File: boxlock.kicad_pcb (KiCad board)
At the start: 2 copper layers, 49.2 x 82.2 mm, 39 parts, among them J2 SOLENOID, J3 USB_B, J4 VEXT, J6 CONN_02X05, J8 KEYPAD, Q1 TIP120, Q2 TIP120, SW1 RESET, U1 LD1117AS33TR, U2 NE555, U3 SAMD21E

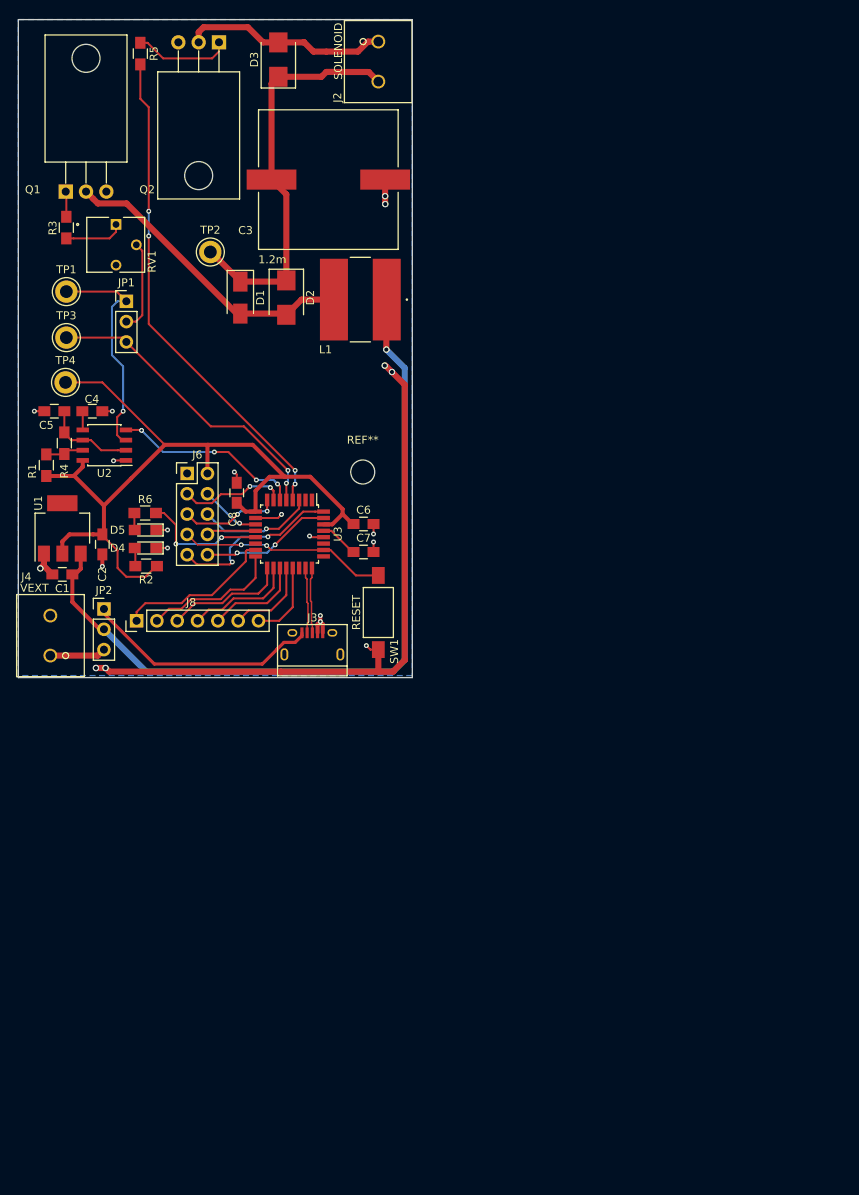
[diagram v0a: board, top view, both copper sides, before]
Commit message: Relayout for rev 1.1.
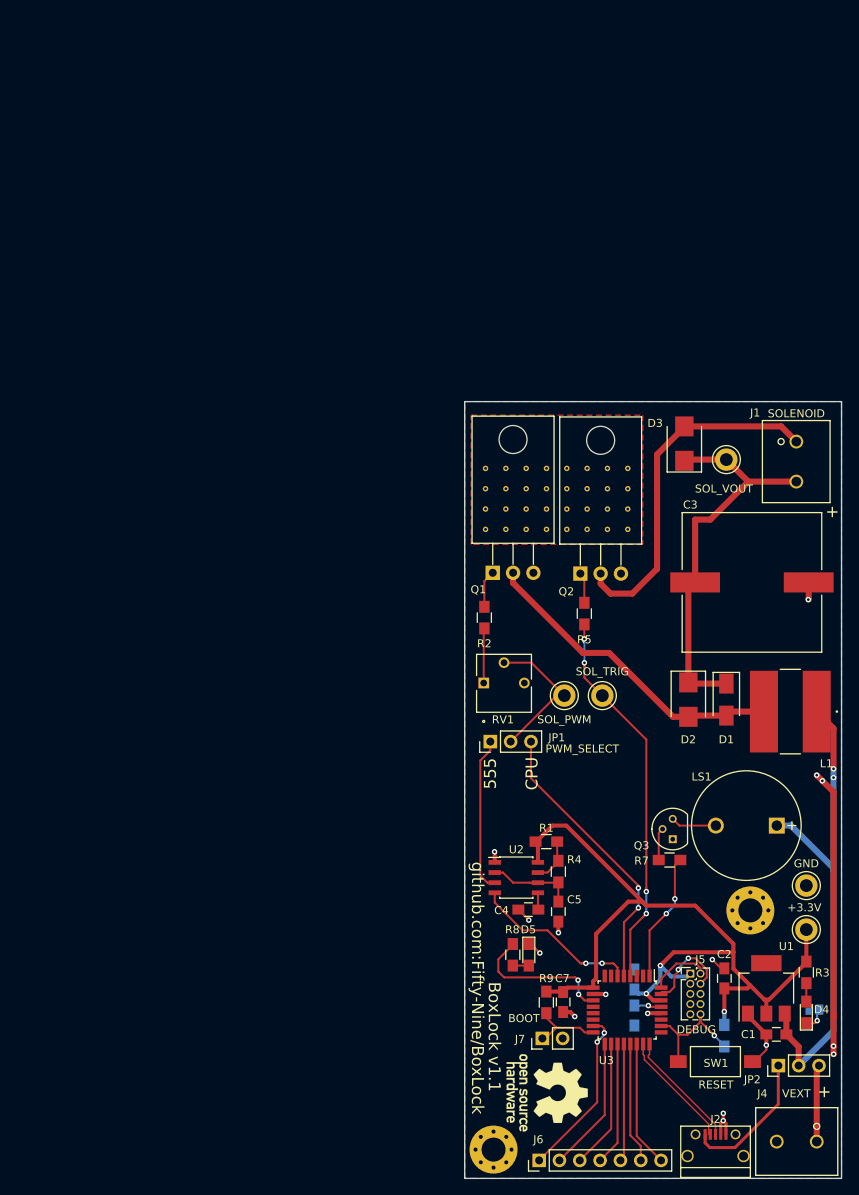
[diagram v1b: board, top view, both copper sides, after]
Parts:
- removed J8: KEYPAD, Pin_Headers:Pin_Header_Straight_1x07_Pitch2.54mm
- removed the REF** at (83.5, 81.8)
- added G***: LOGO, footprints:oshw, F.Cu at (106.6, 159.4)
- added J1: SOLENOID, footprints:282836-2, F.Cu at (137.8, 83.0)
- added J5: DEBUG, Pin_Headers:Pin_Header_Straight_2x05_Pitch1.27mm, F.Cu at (124.5, 144.5)
- added J7: BOOT, Pin_Headers:Pin_Header_Straight_1x02_Pitch2.54mm, F.Cu at (106.0, 152.6)
- added LS1: Buzzer, footprints:CEP-2242, F.Cu at (131.5, 126.0)
- added Q3: 2N3904, TO_SOT_Packages_THT:TO-92_Molded_Narrow, F.Cu at (122.3, 127.7)
- added R7: 2.2k, Resistors_SMD:R_0805_HandSoldering, F.Cu at (121.9, 130.3)
- added R8: 470, Resistors_SMD:R_0805_HandSoldering, F.Cu at (102.3, 142.1)
- added R9: 10k, Resistors_SMD:R_0805_HandSoldering, F.Cu at (106.5, 148.1)
- added REF**: Via_27milx13mil, footprints:Via_27milx13mil, F.Cu at (116.7, 89.0)
- added REF**: Via_27milx13mil, footprints:Via_27milx13mil, F.Cu at (114.1, 86.4)
- added REF**: Via_27milx13mil, footprints:Via_27milx13mil, F.Cu at (111.6, 86.4)
- added REF**: Via_27milx13mil, footprints:Via_27milx13mil, F.Cu at (109.1, 86.4)
- added REF**: Via_27milx13mil, footprints:Via_27milx13mil, F.Cu at (106.5, 86.4)
- added REF**: Via_27milx13mil, footprints:Via_27milx13mil, F.Cu at (104.0, 86.4)
- added REF**: Via_27milx13mil, footprints:Via_27milx13mil, F.Cu at (101.4, 86.4)
- added REF**: Via_27milx13mil, footprints:Via_27milx13mil, F.Cu at (98.9, 86.4)
- added REF**: Via_27milx13mil, footprints:Via_27milx13mil, F.Cu at (116.7, 83.9)
- added REF**: Via_27milx13mil, footprints:Via_27milx13mil, F.Cu at (114.1, 83.9)
- added REF**: Via_27milx13mil, footprints:Via_27milx13mil, F.Cu at (111.6, 83.9)
- added REF**: Via_27milx13mil, footprints:Via_27milx13mil, F.Cu at (114.1, 89.0)
- added REF**: Via_27milx13mil, footprints:Via_27milx13mil, F.Cu at (109.1, 83.9)
- added REF**: Via_27milx13mil, footprints:Via_27milx13mil, F.Cu at (106.5, 83.9)
- added REF**: Via_27milx13mil, footprints:Via_27milx13mil, F.Cu at (104.0, 83.9)
- added REF**: Via_27milx13mil, footprints:Via_27milx13mil, F.Cu at (101.4, 83.9)
- added REF**: Via_27milx13mil, footprints:Via_27milx13mil, F.Cu at (98.9, 83.9)
- added REF**: Via_27milx13mil, footprints:Via_27milx13mil, F.Cu at (116.7, 81.3)
- added REF**: Via_27milx13mil, footprints:Via_27milx13mil, F.Cu at (114.1, 81.3)
- added REF**: Via_27milx13mil, footprints:Via_27milx13mil, F.Cu at (111.6, 81.3)
- added REF**: Via_27milx13mil, footprints:Via_27milx13mil, F.Cu at (109.1, 81.3)
- added REF**: Via_27milx13mil, footprints:Via_27milx13mil, F.Cu at (106.5, 81.3)
- added REF**: Via_27milx13mil, footprints:Via_27milx13mil, F.Cu at (111.6, 89.0)
- added REF**: Via_27milx13mil, footprints:Via_27milx13mil, F.Cu at (104.0, 81.3)
- added REF**: Via_27milx13mil, footprints:Via_27milx13mil, F.Cu at (101.4, 81.3)
- added REF**: Via_27milx13mil, footprints:Via_27milx13mil, F.Cu at (98.9, 81.3)
- added REF**: MountingHole_3mm_Pad_Via, Mounting_Holes:MountingHole_3mm_Pad_Via, F.Cu at (132.0, 136.6)
- added REF**: MountingHole_3mm_Pad_Via, Mounting_Holes:MountingHole_3mm_Pad_Via, F.Cu at (99.9, 166.5)
- added REF**: Via_27milx13mil, footprints:Via_27milx13mil, F.Cu at (109.1, 89.0)
- added REF**: Via_27milx13mil, footprints:Via_27milx13mil, F.Cu at (106.5, 89.0)
- added REF**: Via_27milx13mil, footprints:Via_27milx13mil, F.Cu at (104.0, 89.0)
- added REF**: Via_27milx13mil, footprints:Via_27milx13mil, F.Cu at (101.4, 89.0)
- added REF**: Via_27milx13mil, footprints:Via_27milx13mil, F.Cu at (98.9, 89.0)
- added REF**: Via_27milx13mil, footprints:Via_27milx13mil, F.Cu at (116.7, 86.4)
- added TP5: GND, Measurement_Points:Test_Point_Keystone_5005-5009_Compact, F.Cu at (139.0, 133.5)
- C6, C8: moved to B.Cu
- D4: value D5988 -> D5988-RD
- D5: value D5988 -> D5988-GN
- J2: value SOLENOID -> USB_B; footprint footprints:282836-2 -> footprints:USB_Micro-B-circular
- J3: value USB_B -> LED_EN; footprint Connectors:USB_Micro-B -> Connectors:GS2; moved to B.Cu
- J6: value CONN_02X05 -> KEYPAD; footprint Pin_Headers:Pin_Header_Straight_2x05_Pitch2.54mm -> Pin_Headers:Pin_Header_Straight_1x07_Pitch2.54mm
- R2: value 470 -> 2.2k
- R3: value 2.2k -> 470
- R6: value 470 -> 10k; moved to B.Cu
- TP1: value 555_PWM -> SOL_VOUT
- TP2: value VSOL -> SOL_TRIG
- TP3: value CPU_PWM -> SOL_PWM
- moved J2 139.5 mm to (127.7, 165.9), turned to 0 degrees
- moved R3 131.2 mm to (139.0, 144.3), turned to 90 degrees
- moved TP4 115.1 mm to (139.0, 139.0)
- moved J4 112.1 mm to (135.3, 165.5), turned to 180 degrees
- moved C1 106.2 mm to (135.2, 152.1)
- moved U1 105.1 mm to (134.0, 146.3)
- moved JP2 101.8 mm to (135.5, 156.0), turned to 90 degrees
- moved D4 101.0 mm to (139.0, 149.3), turned to 90 degrees
- moved R6 97.5 mm to (128.8, 152.2), turned to 270 degrees
- moved J6 96.5 mm to (105.6, 167.8), turned to 90 degrees
- moved C2 94.8 mm to (128.8, 145.1), turned to 90 degrees
- moved R5 89.3 mm to (111.2, 99.5)
- moved C5 88.8 mm to (108.0, 136.8), turned to 270 degrees
- moved TP1 85.1 mm to (129.0, 80.2)
- moved C4 82.8 mm to (104.2, 136.5), turned to 180 degrees
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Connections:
- net Net-(D1-Pad2) renamed /SOL_DRV
- C3 pad 1: Net-(C3-Pad1) -> /SOL_VOUT
- C7 pad 1: Net-(C7-Pad1) -> +3V3
- C8 pad 1: +3V3 -> Net-(C8-Pad1)
- D1 pad 1: Net-(C3-Pad1) -> /SOL_VOUT
- D2 pad 1: Net-(C3-Pad1) -> /SOL_VOUT
- D3 pad 1: Net-(C3-Pad1) -> /SOL_VOUT
- D3 pad 2: Net-(D3-Pad2) -> /SOL_COLL
- D4 pad 1: GND -> Net-(D4-Pad1)
- J2 pad 1: Net-(D3-Pad2) -> VBUS
- J2 pad 2: Net-(C3-Pad1) -> USB_D-
- J3 pad 1: VBUS -> Net-(D4-Pad1)
- J3 pad 2: USB_D- -> GND
- J6 pad 1: GND -> Net-(J6-Pad1)
- J6 pad 2: +3V3 -> Net-(J6-Pad2)
- J6 pad 3: PA06 -> Net-(J6-Pad3)
- J6 pad 4: PA08 -> Net-(J6-Pad4)
- J6 pad 5: PA07 -> Net-(J6-Pad5)
- J6 pad 6: PA02 -> Net-(J6-Pad6)
- Q2 pad 2: Net-(D3-Pad2) -> /SOL_COLL
- R2 pad 1: +3V3 -> Net-(Q1-Pad1)
- R2 pad 2: Net-(D4-Pad2) -> Net-(R2-Pad2)
- R3 pad 1: Net-(Q1-Pad1) -> Net-(D4-Pad2)
- R3 pad 2: Net-(R3-Pad2) -> +3V3
- R6 pad 1: Net-(D5-Pad2) -> +3V3
- R6 pad 2: Net-(R6-Pad2) -> ~RESET
- RV1 pad 1: Net-(R3-Pad2) -> Net-(R2-Pad2)
- SW1 pad 2: Net-(J6-Pad7) -> ~RESET
- TP1 pad 1: 555_PWM -> /SOL_VOUT
- TP2 pad 1: Net-(C3-Pad1) -> SOL_TRIG
- TP3 pad 1: CPU_PWM -> SOL_PWM
- U3 pad 1: (no net) -> BUZZ
- U3 pad 11: PA08 -> Net-(R8-Pad2)
- U3 pad 12: PA09 -> (no net)
- U3 pad 13: Net-(R6-Pad2) -> (no net)
- U3 pad 15: Net-(J8-Pad1) -> Net-(J6-Pad1)
- U3 pad 16: Net-(J8-Pad2) -> BOOT
- U3 pad 17: Net-(J8-Pad3) -> Net-(J6-Pad2)
- U3 pad 18: Net-(J8-Pad4) -> Net-(J6-Pad3)
- U3 pad 19: Net-(J8-Pad5) -> Net-(J6-Pad4)
- U3 pad 20: Net-(J8-Pad6) -> Net-(J6-Pad5)
- U3 pad 21: Net-(J8-Pad7) -> Net-(J6-Pad6)
- U3 pad 22: (no net) -> Net-(J6-Pad7)
- U3 pad 26: Net-(J6-Pad7) -> ~RESET
- U3 pad 29: Net-(C7-Pad1) -> Net-(C8-Pad1)
- U3 pad 3: PA02 -> (no net)
- U3 pad 7: PA06 -> (no net)
- U3 pad 8: PA07 -> (no net)
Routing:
- net Net-(C3-Pad1): track 50.8 -> 0.00 mm
- net /SOL_VOUT: track 0.00 -> 49.3 mm
- net GND: track 109.8 -> 63.8 mm, vias 21 -> 16
- net /SOL_COLL: track 0.00 -> 44.1 mm
- net +BATT: track 98.5 -> 63.7 mm, vias 1 -> 2
- net Net-(D3-Pad2): track 25.8 -> 0.00 mm
- net Net-(J6-Pad1): track 0.00 -> 21.4 mm, vias 0 -> 2
- net Net-(J8-Pad1): track 19.9 -> 0.00 mm
- net Net-(R8-Pad2): track 0.00 -> 18.5 mm, vias 0 -> 2
- net Net-(J8-Pad2): track 17.2 -> 0.00 mm
- net Net-(J6-Pad2): track 0.00 -> 16.9 mm
- net Net-(J6-Pad3): track 0.00 -> 16.2 mm
- net BUZZ: track 0.00 -> 16.1 mm, vias 0 -> 2
- net Net-(R6-Pad2): track 15.8 -> 0.00 mm, vias 2 -> 0
- net ~RESET: track 0.00 -> 15.6 mm, vias 0 -> 1
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- added copper zone on F.Cu, net GND
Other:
- board size 49.2 x 82.2 mm -> 47.1 x 97.1 mm
- net class 3.3V Dist added: clearance 0.1524, trace_width 0.508, via_dia 0.6858, via_drill 0.3302
- net class Batt. Dist added: clearance 0.381, trace_width 0.762, via_dia 0.6858, via_drill 0.3302
- net class Default: clearance 0.2 -> 0.1524; via_dia 0.6096 -> 0.6858; via_drill 0.3048 -> 0.3302
- rule trace_clearance: 0.2 -> 0.1524
- rule via_min_drill: 0.3048 -> 0.3302
- rule via_min_size: 0.6096 -> 0.6858
- board text added: "+"
- board text added: "555"
- board text added: "BoxLock v1.1"
- board text added: "CPU"
- board text added: "github.com:Fifty-Nine/BoxLock"
